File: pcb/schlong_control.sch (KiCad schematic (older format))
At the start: 28 parts, among them P1 Power Connector, P2 Data Connector, U1 74HC595, U2 MOC3063M, U3 MOC3063M, U4 MOC3063M, U5 MOC3063M, U6 MOC3063M

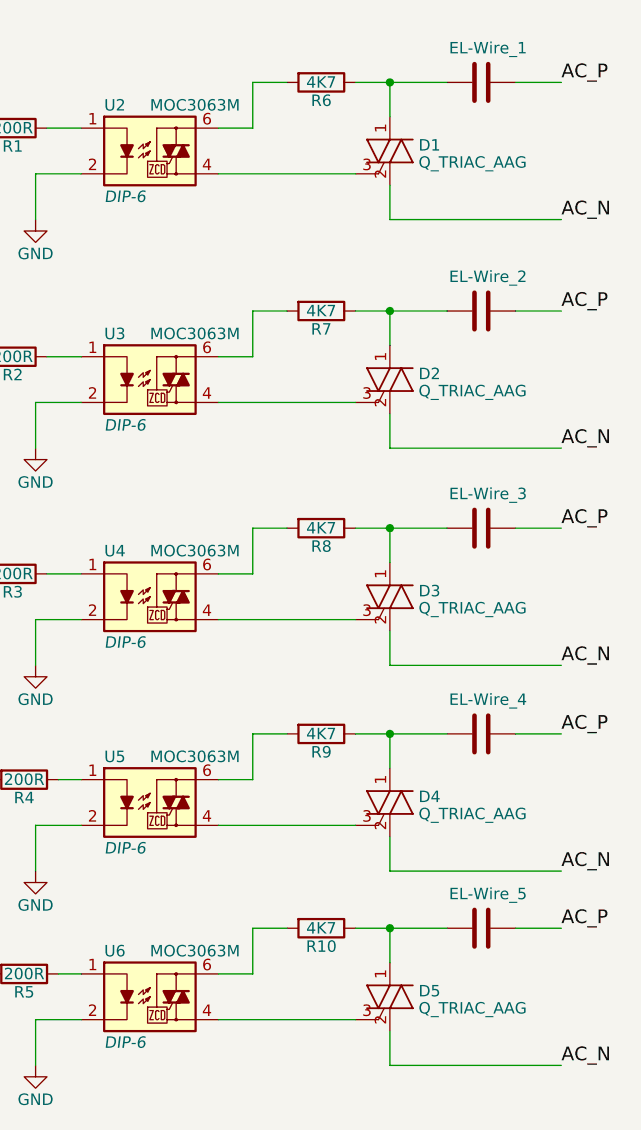
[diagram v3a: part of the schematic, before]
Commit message: add resistors to neutral, adjust values
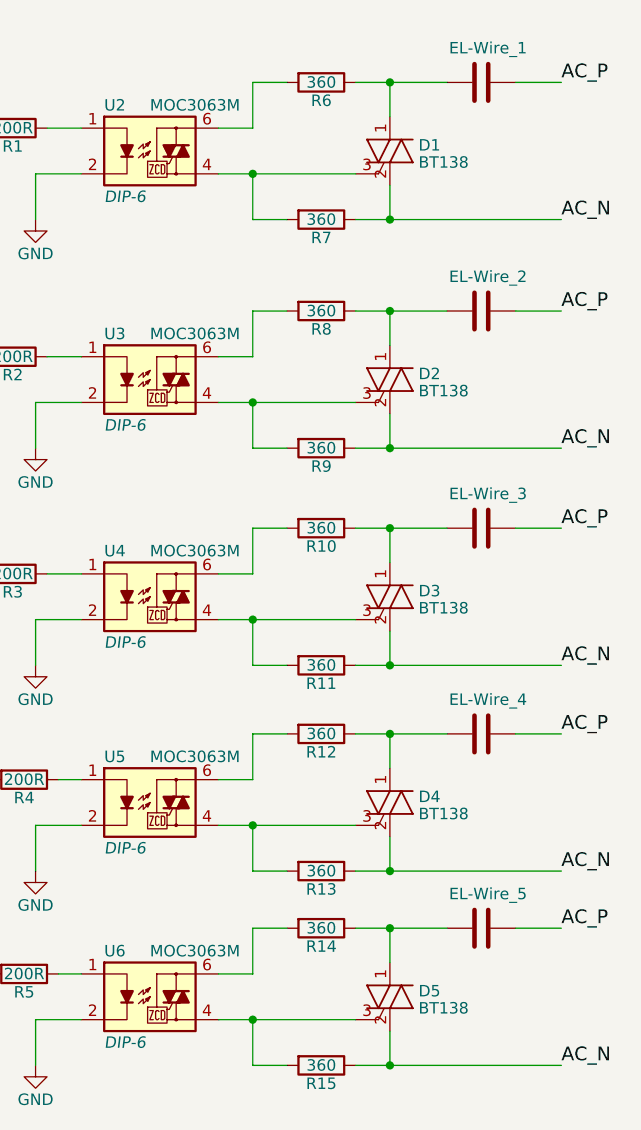
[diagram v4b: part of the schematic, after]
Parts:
- added R11, R13, R15, R7, R9: 360, symbol R
- D1, D2, D3, D4, D5: value Q_TRIAC_AAG -> BT138
- R10: renamed from R8; value 4K7 -> 360
- R12: renamed from R9; value 4K7 -> 360
- R14: renamed from R10; value 4K7 -> 360
- R6: value 4K7 -> 360
- R8: renamed from R7; value 4K7 -> 360
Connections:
- net AC_N: now also R11.1, R13.1, R15.1, R7.1, R9.1
- net at D1.3 (G), U2.4: now also R7.2
- net at D2.3 (G), U3.4: now also R9.2
- net at D3.3 (G), U4.4: now also R11.2
- net at D4.3 (G), U5.4: now also R13.2
- net at D5.3 (G), U6.4: now also R15.2
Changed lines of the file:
@@
 P 6400 1250
 F 0 "D1" H 6525 1275 50  0000 L CNN
-F 1 "Q_TRIAC_AAG" H 6525 1200 50  0000 L CNN
+F 1 "BT138" H 6525 1200 50  0000 L CNN
 F 2 "" V 6475 1275 50  0000 C CNN
 F 3 "" V 6400 1250 50  0000 C CNN
@@
 P 6100 950
 F 0 "R6" V 6180 950 50  0000 C CNN
-F 1 "4K7" V 6100 950 50  0000 C CNN
+F 1 "360" V 6100 950 50  0000 C CNN
 F 2 "" V 6030 950 50  0000 C CNN
 F 3 "" H 6100 950 50  0000 C CNN
@@
 AC_P
 $Comp
-L GND #PWR7
+L GND #PWR01
 U 1 1 58A93B28
 P 4850 1550
-F 0 "#PWR7" H 4850 1300 50  0001 C CNN
+F 0 "#PWR01" H 4850 1300 50  0001 C CNN
 F 1 "GND" H 4850 1400 50  0000 C CNN
 F 2 "" H 4850 1550 50  0000 C CNN
@@
 P 6400 2250
 F 0 "D2" H 6525 2275 50  0000 L CNN
-F 1 "Q_TRIAC_AAG" H 6525 2200 50  0000 L CNN
+F 1 "BT138" H 6525 2200 50  0000 L CNN
 F 2 "" V 6475 2275 50  0000 C CNN
 F 3 "" V 6400 2250 50  0000 C CNN
@@
 $EndComp
 $Comp
-L R R7
+L R R8
 U 1 1 58A941A9
 P 6100 1950
-F 0 "R7" V 6180 1950 50  0000 C CNN
-F 1 "4K7" V 6100 1950 50  0000 C CNN
+F 0 "R8" V 6180 1950 50  0000 C CNN
+F 1 "360" V 6100 1950 50  0000 C CNN
 F 2 "" V 6030 1950 50  0000 C CNN
 F 3 "" H 6100 1950 50  0000 C CNN
@@
 AC_P
 $Comp
-L GND #PWR8
+L GND #PWR02
 U 1 1 58A941CA
 P 4850 2550
-F 0 "#PWR8" H 4850 2300 50  0001 C CNN
+F 0 "#PWR02" H 4850 2300 50  0001 C CNN
 F 1 "GND" H 4850 2400 50  0000 C CNN
 F 2 "" H 4850 2550 50  0000 C CNN
@@
 P 6400 3200
 F 0 "D3" H 6525 3225 50  0000 L CNN
-F 1 "Q_TRIAC_AAG" H 6525 3150 50  0000 L CNN
+F 1 "BT138" H 6525 3150 50  0000 L CNN
 F 2 "" V 6475 3225 50  0000 C CNN
 F 3 "" V 6400 3200 50  0000 C CNN
@@
 $EndComp
 $Comp
-L R R8
+L R R10
 U 1 1 58A94276
 P 6100 2900
-F 0 "R8" V 6180 2900 50  0000 C CNN
-F 1 "4K7" V 6100 2900 50  0000 C CNN
+F 0 "R10" V 6180 2900 50  0000 C CNN
+F 1 "360" V 6100 2900 50  0000 C CNN
 F 2 "" V 6030 2900 50  0000 C CNN
 F 3 "" H 6100 2900 50  0000 C CNN
@@
 AC_P
 $Comp
-L GND #PWR9
+L GND #PWR03
 U 1 1 58A94296
 P 4850 3500
-F 0 "#PWR9" H 4850 3250 50  0001 C CNN
+F 0 "#PWR03" H 4850 3250 50  0001 C CNN
 F 1 "GND" H 4850 3350 50  0000 C CNN
 F 2 "" H 4850 3500 50  0000 C CNN
@@
 P 6400 4100
 F 0 "D4" H 6525 4125 50  0000 L CNN
-F 1 "Q_TRIAC_AAG" H 6525 4050 50  0000 L CNN
+F 1 "BT138" H 6525 4050 50  0000 L CNN
 F 2 "" V 6475 4125 50  0000 C CNN
 F 3 "" V 6400 4100 50  0000 C CNN
@@
 $EndComp
 $Comp
-L R R9
+L R R12
 U 1 1 58A94353
 P 6100 3800
-F 0 "R9" V 6180 3800 50  0000 C CNN
-F 1 "4K7" V 6100 3800 50  0000 C CNN
+F 0 "R12" V 6180 3800 50  0000 C CNN
+F 1 "360" V 6100 3800 50  0000 C CNN
 F 2 "" V 6030 3800 50  0000 C CNN
 F 3 "" H 6100 3800 50  0000 C CNN
@@
 AC_P
 $Comp
-L GND #PWR10
+L GND #PWR04
 U 1 1 58A94373
 P 4850 4400
-F 0 "#PWR10" H 4850 4150 50  0001 C CNN
+F 0 "#PWR04" H 4850 4150 50  0001 C CNN
 F 1 "GND" H 4850 4250 50  0000 C CNN
 F 2 "" H 4850 4400 50  0000 C CNN
@@
 P 6400 4950
 F 0 "D5" H 6525 4975 50  0000 L CNN
-F 1 "Q_TRIAC_AAG" H 6525 4900 50  0000 L CNN
+F 1 "BT138" H 6525 4900 50  0000 L CNN
 F 2 "" V 6475 4975 50  0000 C CNN
 F 3 "" V 6400 4950 50  0000 C CNN
@@
 $EndComp
 $Comp
-L R R10
+L R R14
 U 1 1 58A94816
 P 6100 4650
-F 0 "R10" V 6180 4650 50  0000 C CNN
-F 1 "4K7" V 6100 4650 50  0000 C CNN
+F 0 "R14" V 6180 4650 50  0000 C CNN
+F 1 "360" V 6100 4650 50  0000 C CNN
 F 2 "" V 6030 4650 50  0000 C CNN
 F 3 "" H 6100 4650 50  0000 C CNN
@@
 AC_P
 $Comp
-L GND #PWR11
+L GND #PWR05
 U 1 1 58A94836
 P 4850 5250
-F 0 "#PWR11" H 4850 5000 50  0001 C CNN
+F 0 "#PWR05" H 4850 5000 50  0001 C CNN
 F 1 "GND" H 4850 5100 50  0000 C CNN
 F 2 "" H 4850 5250 50  0000 C CNN
@@
 NoConn ~ 4000 3800
 $Comp
-L VCC #PWR3
+L VCC #PWR06
 U 1 1 58A979A6
 P 1750 2700
-F 0 "#PWR3" H 1750 2550 50  0001 C CNN
+F 0 "#PWR06" H 1750 2550 50  0001 C CNN
 F 1 "VCC" H 1750 2850 50  0000 C CNN
 F 2 "" H 1750 2700 50  0000 C CNN
@@
 $EndComp
 $Comp
-L GND #PWR5
+L GND #PWR07
 U 1 1 58A98202
 P 2450 3700
-F 0 "#PWR5" H 2450 3450 50  0001 C CNN
+F 0 "#PWR07" H 2450 3450 50  0001 C CNN
 F 1 "GND" H 2450 3550 50  0000 C CNN
 F 2 "" H 2450 3700 50  0000 C CNN
@@
 $EndComp
 $Comp
-L VCC #PWR2
+L VCC #PWR08
 U 1 1 58A90835
 P 900 1050
-F 0 "#PWR2" H 900 900 50  0001 C CNN
+F 0 "#PWR08" H 900 900 50  0001 C CNN
 F 1 "VCC" H 900 1200 50  0000 C CNN
 F 2 "" H 900 1050 50  0000 C CNN
@@
 $EndComp
 $Comp
-L +5V #PWR1
+L +5V #PWR09
 U 1 1 58A9087D
 P 900 900
-F 0 "#PWR1" H 900 750 50  0001 C CNN
+F 0 "#PWR09" H 900 750 50  0001 C CNN
 F 1 "+5V" H 900 1040 50  0000 C CNN
 F 2 "" H 900 900 50  0000 C CNN
@@
 $EndComp
 $Comp
-L PWR_FLAG #FLG1
+L PWR_FLAG #FLG010
 U 1 1 58A90FC6
 P 1400 900
-F 0 "#FLG1" H 1400 995 50  0001 C CNN
+F 0 "#FLG010" H 1400 995 50  0001 C CNN
 F 1 "PWR_FLAG" H 1400 1080 50  0000 C CNN
 F 2 "" H 1400 900 50  0000 C CNN
@@
 $EndComp
 $Comp
-L PWR_FLAG #FLG2
+L PWR_FLAG #FLG011
 U 1 1 58A91E89
 P 1850 900
-F 0 "#FLG2" H 1850 995 50  0001 C CNN
+F 0 "#FLG011" H 1850 995 50  0001 C CNN
 F 1 "PWR_FLAG" H 1850 1080 50  0000 C CNN
 F 2 "" H 1850 900 50  0000 C CNN
@@
 $EndComp
 $Comp
-L GND #PWR4
+L GND #PWR012
 U 1 1 58A9369D
 P 1850 1050
-F 0 "#PWR4" H 1850 800 50  0001 C CNN
+F 0 "#PWR012" H 1850 800 50  0001 C CNN
 F 1 "GND" H 1850 900 50  0000 C CNN
 F 2 "" H 1850 1050 50  0000 C CNN
@@
 AC_N
 $Comp
-L GND #PWR6
+L GND #PWR013
 U 1 1 58A95862
 P 3500 1800
-F 0 "#PWR6" H 3500 1550 50  0001 C CNN
+F 0 "#PWR013" H 3500 1550 50  0001 C CNN
 F 1 "GND" H 3500 1650 50  0000 C CNN
 F 2 "" H 3500 1800 50  0000 C CNN
@@
 	2600 1150 2800 1150
 Wire Wire Line
-	6400 1550 7150 1550
-Wire Wire Line
-	6400 5250 7150 5250
-Wire Wire Line
-	6400 4400 7150 4400
-Wire Wire Line
-	6400 3500 7150 3500
-Wire Wire Line
-	6400 2550 7150 2550
+	6250 1550 7150 1550
+Wire Wire Line
+	6250 5250 7150 5250
+Wire Wire Line
+	6250 4400 7150 4400
+Wire Wire Line
+	6250 3500 7150 3500
+Wire Wire Line
+	6250 2550 7150 2550
 $Comp
 L MOC3063M U2
@@
 Wire Wire Line
 	4950 4850 5050 4850
+$Comp
+L R R7
+U 1 1 58C9C1D6
+P 6100 1550
+F 0 "R7" V 6180 1550 50  0000 C CNN
+F 1 "360" V 6100 1550 50  0000 C CNN
+F 2 "" V 6030 1550 50  0000 C CNN
+F 3 "" H 6100 1550 50  0000 C CNN
+	1    6100 1550
+	0    1    1    0
+$EndComp
+$Comp
+L R R9
+U 1 1 58C9C4EE
+P 6100 2550
+F 0 "R9" V 6180 2550 50  0000 C CNN
+F 1 "360" V 6100 2550 50  0000 C CNN
+F 2 "" V 6030 2550 50  0000 C CNN
+F 3 "" H 6100 2550 50  0000 C CNN
+	1    6100 2550
+	0    1    1    0
+$EndComp
+$Comp
+L R R11
+U 1 1 58C9CA36
+P 6100 3500
+F 0 "R11" V 6180 3500 50  0000 C CNN
+F 1 "360" V 6100 3500 50  0000 C CNN
+F 2 "" V 6030 3500 50  0000 C CNN
+F 3 "" H 6100 3500 50  0000 C CNN
+	1    6100 3500
+	0    1    1    0
+$EndComp
+$Comp
+L R R13
+U 1 1 58C9D53C
+P 6100 4400
+F 0 "R13" V 6180 4400 50  0000 C CNN
+F 1 "360" V 6100 4400 50  0000 C CNN
+F 2 "" V 6030 4400 50  0000 C CNN
+F 3 "" H 6100 4400 50  0000 C CNN
+	1    6100 4400
+	0    1    1    0
+$EndComp
+$Comp
+L R R15
+U 1 1 58C9D61A
+P 6100 5250
+F 0 "R15" V 6180 5250 50  0000 C CNN
+F 1 "360" V 6100 5250 50  0000 C CNN
+F 2 "" V 6030 5250 50  0000 C CNN
+F 3 "" H 6100 5250 50  0000 C CNN
+	1    6100 5250
+	0    1    1    0
+$EndComp
+Connection ~ 6400 5250
+Wire Wire Line
+	5800 5050 5800 5250
+Wire Wire Line
+	5800 5250 5950 5250
+Connection ~ 5800 5050
+Wire Wire Line
+	5800 4200 5800 4400
+Wire Wire Line
+	5800 4400 5950 4400
+Connection ~ 5800 4200
+Wire Wire Line
+	5800 3300 5800 3500
+Wire Wire Line
+	5800 3500 5950 3500
+Connection ~ 5800 3300
+Wire Wire Line
+	5800 2350 5800 2550
+Wire Wire Line
+	5800 2550 5950 2550
+Connection ~ 5800 2350
+Wire Wire Line
+	5800 1350 5800 1550
+Wire Wire Line
+	5800 1550 5950 1550
+Connection ~ 5800 1350
+Connection ~ 6400 1550
+Connection ~ 6400 2550
+Connection ~ 6400 3500
+Connection ~ 6400 4400
 $EndSCHEMATC

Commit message: finished circuit
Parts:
- removed P2: Data Connector, symbol CONN_02X02
- added C?: 0.22µF, symbol C
- added P1: Input, symbol CONN_02X05
- added P3: Output, symbol CONN_02X05
- added U7: LM7805, symbol LM7805
- P2: renamed from P1; value Power Connector -> Power Connector (120V AC)
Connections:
- net GND: now also C?.2, P1.10 (P10), P1.9 (P9), P3.10 (P10), P3.9 (P9), U7.GND
- net MOSI: now also P1.3 (P3), P1.4 (P4)
- net SCK: now also P1.5 (P5), P1.6 (P6), P3.5 (P5), P3.6 (P6)
- net ~QH: now reaches U1.9 (~QH)
- net ~QH: now also P3.3 (P3), P3.4 (P4)
- net +5V renamed VCC
- net VCC: now also U7.VO
- net ~SCHLONG_SELECT renamed ~LATCH
- net ~LATCH: now also P1.7 (P7), P1.8 (P8), P3.7 (P7), P3.8 (P8)
- new net +12V: C?.1, P1.1 (P1), P1.2 (P2), P3.1 (P1), P3.2 (P2), U7.VI
- no-connect marks 4 -> 3
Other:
- moved on the sheet: P2

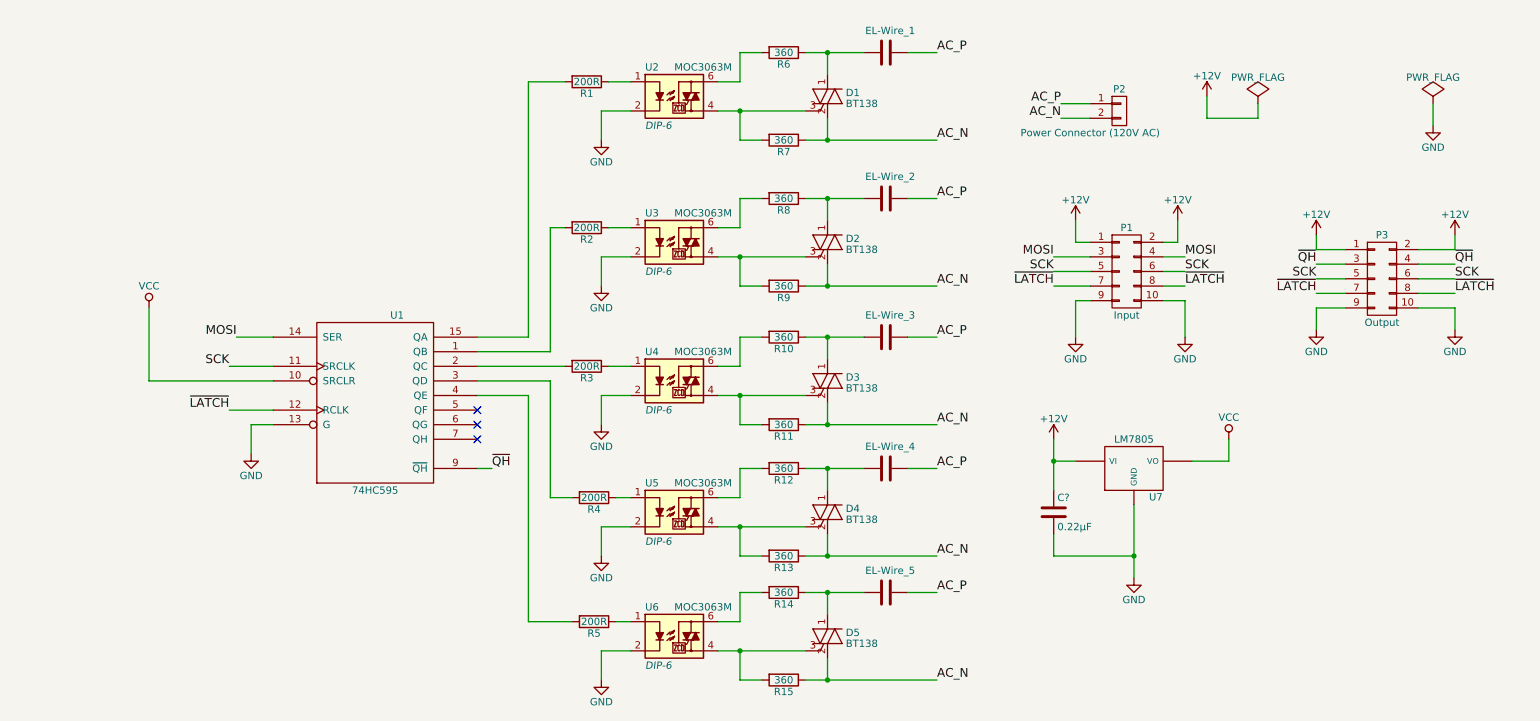
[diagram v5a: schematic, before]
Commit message: rev1: use 1k resistors on MOC3063 LED / corrected pinout on BT138
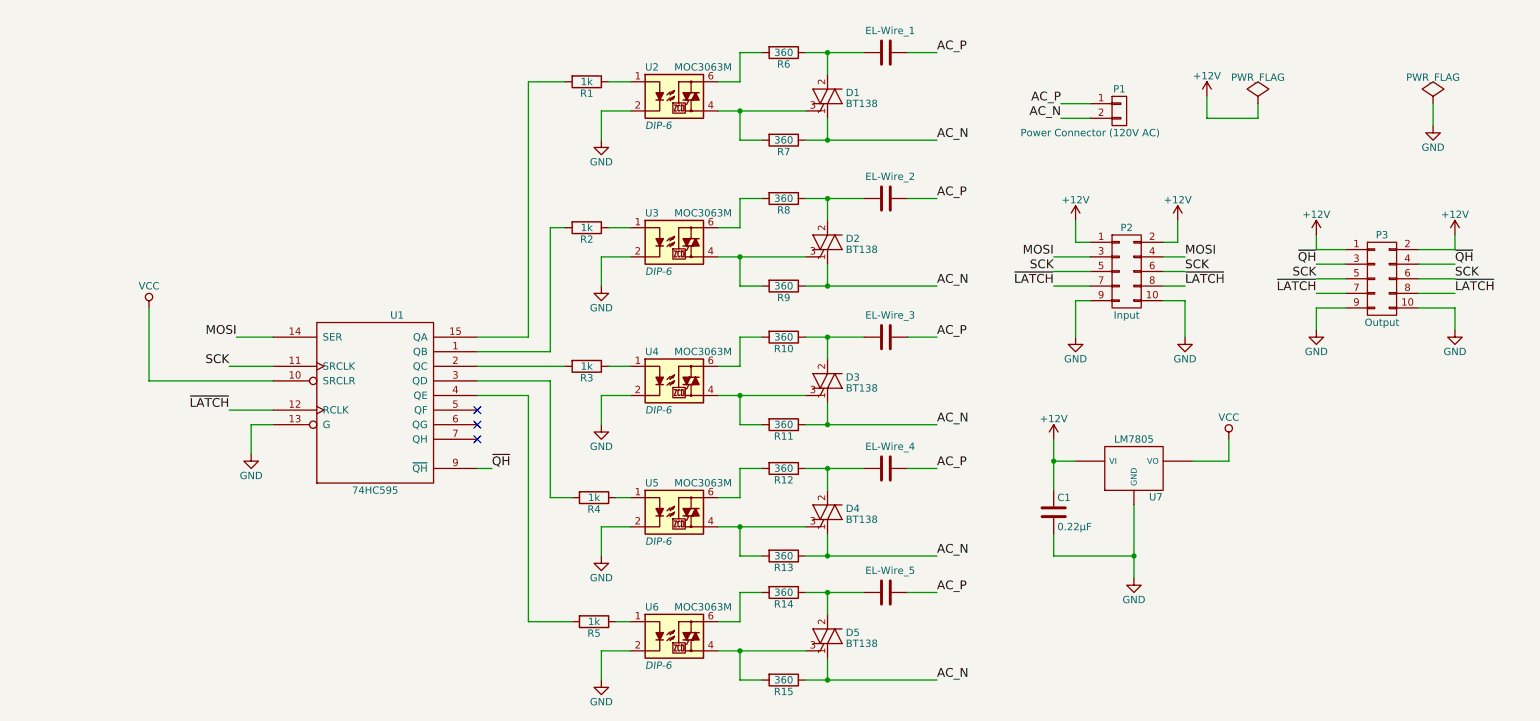
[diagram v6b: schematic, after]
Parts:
- removed D1, D2, D3, D4, D5: BT138, symbol Q_TRIAC_AAG
- added D1, D2, D3, D4, D5: BT138, symbol BT138
- R1, R2, R3, R4, R5: value 200R -> 1k
- gave numbers to parts that had none: 1
- renumbered P2 to P1, P1 to P2
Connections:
- net AC_N: now also D1.1 (T1), D2.1 (T1), D3.1 (T1), D4.1 (T1), D5.1 (T1)
- net at EL-Wire_1.1, R6.1: now also D1.2 (T2)
- net at R7.2, U2.4: now also D1.3 (G)
- net at EL-Wire_2.1, R8.1: now also D2.2 (T2)
- net at R9.2, U3.4: now also D2.3 (G)
- net at EL-Wire_3.1, R10.1: now also D3.2 (T2)
- net at R11.2, U4.4: now also D3.3 (G)
- net at EL-Wire_4.1, R12.1: now also D4.2 (T2)
- net at R13.2, U5.4: now also D4.3 (G)
- net at EL-Wire_5.1, R14.1: now also D5.2 (T2)
- net at R15.2, U6.4: now also D5.3 (G)
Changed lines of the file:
@@
 LIBS:contrib
 LIBS:valves
+LIBS:bt138
 LIBS:schlong_control-cache
 EELAYER 25 0
@@
 Title "Schlong Module Circuit"
 Date "2017-03-16"
-Rev "-"
+Rev "1"
 Comp "coon@c-base.org"
 Comment1 ""
@@
 Comment4 ""
 $EndDescr
-$Comp
-L Q_TRIAC_AAG D1
-U 1 1 58A8BC5D
-P 6400 1250
-F 0 "D1" H 6525 1275 50  0000 L CNN
-F 1 "BT138" H 6525 1200 50  0000 L CNN
-F 2 "" V 6475 1275 50  0000 C CNN
-F 3 "" V 6400 1250 50  0000 C CNN
-	1    6400 1250
-	1    0    0    -1
-$EndComp
 $Comp
 L R R6
@@
 AC_N
 $Comp
-L Q_TRIAC_AAG D2
-U 1 1 58A941A3
-P 6400 2250
-F 0 "D2" H 6525 2275 50  0000 L CNN
-F 1 "BT138" H 6525 2200 50  0000 L CNN
-F 2 "" V 6475 2275 50  0000 C CNN
-F 3 "" V 6400 2250 50  0000 C CNN
-	1    6400 2250
-	1    0    0    -1
-$EndComp
-$Comp
 L R R8
 U 1 1 58A941A9
@@
 AC_N
 $Comp
-L Q_TRIAC_AAG D3
-U 1 1 58A94270
-P 6400 3200
-F 0 "D3" H 6525 3225 50  0000 L CNN
-F 1 "BT138" H 6525 3150 50  0000 L CNN
-F 2 "" V 6475 3225 50  0000 C CNN
-F 3 "" V 6400 3200 50  0000 C CNN
-	1    6400 3200
-	1    0    0    -1
-$EndComp
-$Comp
 L R R10
 U 1 1 58A94276
@@
 AC_N
 $Comp
-L Q_TRIAC_AAG D4
-U 1 1 58A9434D
-P 6400 4100
-F 0 "D4" H 6525 4125 50  0000 L CNN
-F 1 "BT138" H 6525 4050 50  0000 L CNN
-F 2 "" V 6475 4125 50  0000 C CNN
-F 3 "" V 6400 4100 50  0000 C CNN
-	1    6400 4100
-	1    0    0    -1
-$EndComp
-$Comp
 L R R12
 U 1 1 58A94353
@@
 Text Label 7150 4400 0    60   ~ 0
 AC_N
-$Comp
-L Q_TRIAC_AAG D5
-U 1 1 58A94810
-P 6400 4950
-F 0 "D5" H 6525 4975 50  0000 L CNN
-F 1 "BT138" H 6525 4900 50  0000 L CNN
-F 2 "" V 6475 4975 50  0000 C CNN
-F 3 "" V 6400 4950 50  0000 C CNN
-	1    6400 4950
-	1    0    0    -1
-$EndComp
 $Comp
 L R R14
@@
 $EndComp
 $Comp
-L CONN_01X02 P2
+L CONN_01X02 P1
 U 1 1 58A95478
 P 8400 1350
-F 0 "P2" H 8400 1500 50  0000 C CNN
+F 0 "P1" H 8400 1500 50  0000 C CNN
 F 1 "Power Connector (120V AC)" H 8200 1200 50  0000 C CNN
 F 2 "" H 8400 1350 50  0000 C CNN
@@
 P 4750 1150
 F 0 "R1" V 4830 1150 50  0000 C CNN
-F 1 "200R" V 4750 1150 50  0000 C CNN
+F 1 "1k" V 4750 1150 50  0000 C CNN
 F 2 "" V 4680 1150 50  0000 C CNN
 F 3 "" H 4750 1150 50  0000 C CNN
@@
 P 4750 2150
 F 0 "R2" V 4830 2150 50  0000 C CNN
-F 1 "200R" V 4750 2150 50  0000 C CNN
+F 1 "1k" V 4750 2150 50  0000 C CNN
 F 2 "" V 4680 2150 50  0000 C CNN
 F 3 "" H 4750 2150 50  0000 C CNN
@@
 P 4750 3100
 F 0 "R3" V 4830 3100 50  0000 C CNN
-F 1 "200R" V 4750 3100 50  0000 C CNN
+F 1 "1k" V 4750 3100 50  0000 C CNN
 F 2 "" V 4680 3100 50  0000 C CNN
 F 3 "" H 4750 3100 50  0000 C CNN
@@
 P 4800 4000
 F 0 "R4" V 4880 4000 50  0000 C CNN
-F 1 "200R" V 4800 4000 50  0000 C CNN
+F 1 "1k" V 4800 4000 50  0000 C CNN
 F 2 "" V 4730 4000 50  0000 C CNN
 F 3 "" H 4800 4000 50  0000 C CNN
@@
 P 4800 4850
 F 0 "R5" V 4880 4850 50  0000 C CNN
-F 1 "200R" V 4800 4850 50  0000 C CNN
+F 1 "1k" V 4800 4850 50  0000 C CNN
 F 2 "" V 4730 4850 50  0000 C CNN
 F 3 "" H 4800 4850 50  0000 C CNN
@@
 $EndComp
 $Comp
-L CONN_02X05 P1
+L CONN_02X05 P2
 U 1 1 58C9CEB2
 P 8450 2450
-F 0 "P1" H 8450 2750 50  0000 C CNN
+F 0 "P2" H 8450 2750 50  0000 C CNN
 F 1 "Input" H 8450 2150 50  0000 C CNN
 F 2 "" H 8450 1250 50  0000 C CNN
@@
 	8900 3750 9150 3750
 $Comp
-L C C?
+L C C1
 U 1 1 58CB259E
 P 7950 4100
-F 0 "C?" H 7975 4200 50  0000 L CNN
+F 0 "C1" H 7975 4200 50  0000 L CNN
 F 1 "0.22µF" H 7975 4000 50  0000 L CNN
 F 2 "" H 7988 3950 50  0000 C CNN
@@
 	7950 4400 8500 4400
 Connection ~ 8500 4400
+$Comp
+L BT138 D1
+U 1 1 58CBA261
+P 6400 1250
+F 0 "D1" H 6525 1275 50  0000 L CNN
+F 1 "BT138" H 6525 1200 50  0000 L CNN
+F 2 "" V 6475 1275 50  0000 C CNN
+F 3 "" V 6400 1250 50  0000 C CNN
+	1    6400 1250
+	1    0    0    -1
+$EndComp
+$Comp
+L BT138 D2
+U 1 1 58CBA46D
+P 6400 2250
+F 0 "D2" H 6525 2275 50  0000 L CNN
+F 1 "BT138" H 6525 2200 50  0000 L CNN
+F 2 "" V 6475 2275 50  0000 C CNN
+F 3 "" V 6400 2250 50  0000 C CNN
+	1    6400 2250
+	1    0    0    -1
+$EndComp
+$Comp
+L BT138 D3
+U 1 1 58CBA540
+P 6400 3200
+F 0 "D3" H 6525 3225 50  0000 L CNN
+F 1 "BT138" H 6525 3150 50  0000 L CNN
+F 2 "" V 6475 3225 50  0000 C CNN
+F 3 "" V 6400 3200 50  0000 C CNN
+	1    6400 3200
+	1    0    0    -1
+$EndComp
+$Comp
+L BT138 D4
+U 1 1 58CBA60D
+P 6400 4100
+F 0 "D4" H 6525 4125 50  0000 L CNN
+F 1 "BT138" H 6525 4050 50  0000 L CNN
+F 2 "" V 6475 4125 50  0000 C CNN
+F 3 "" V 6400 4100 50  0000 C CNN
+	1    6400 4100
+	1    0    0    -1
+$EndComp
+$Comp
+L BT138 D5
+U 1 1 58CBA6BA
+P 6400 4950
+F 0 "D5" H 6525 4975 50  0000 L CNN
+F 1 "BT138" H 6525 4900 50  0000 L CNN
+F 2 "" V 6475 4975 50  0000 C CNN
+F 3 "" V 6400 4950 50  0000 C CNN
+	1    6400 4950
+	1    0    0    -1
+$EndComp
 $EndSCHEMATC
